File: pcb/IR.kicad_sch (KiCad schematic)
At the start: 6 parts, among them Q10 BS170, Q11 TEFT4300

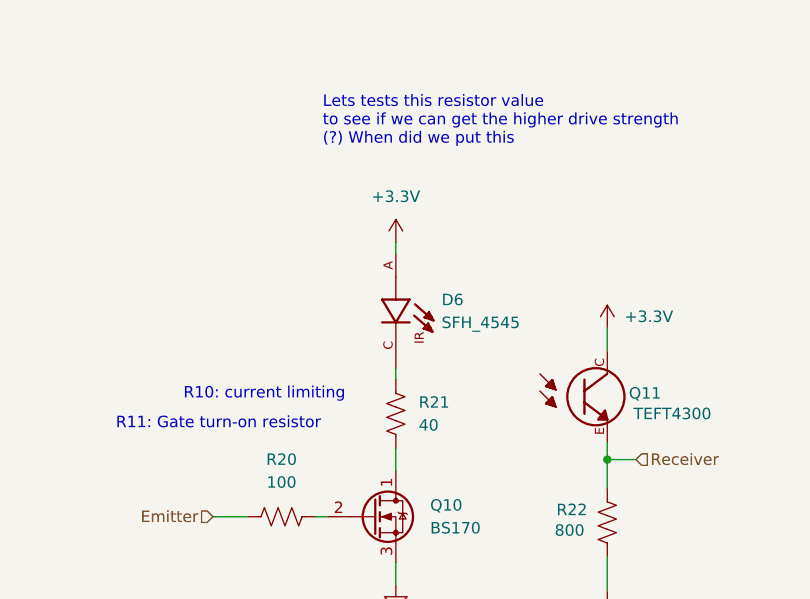
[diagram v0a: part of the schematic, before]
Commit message: changed voltage and resistor values for emitters
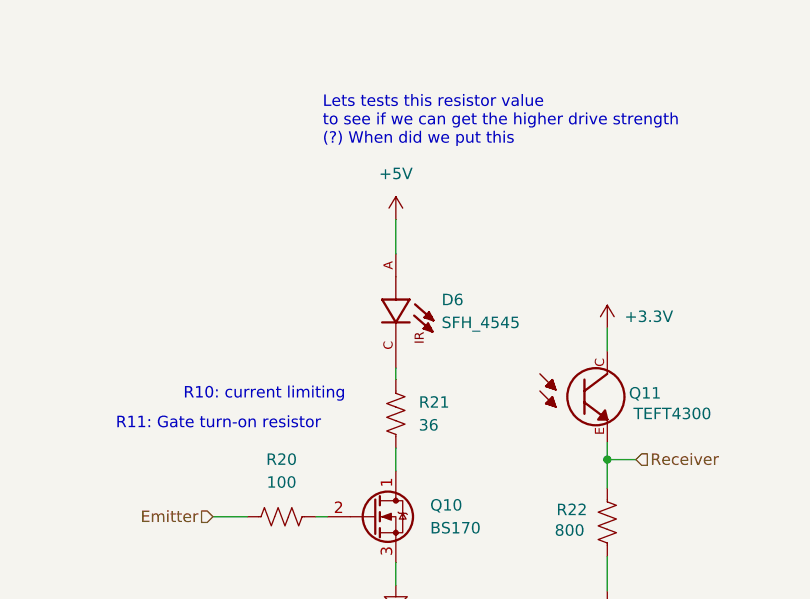
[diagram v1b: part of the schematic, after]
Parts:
- R21: value 40 -> 36
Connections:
- net +3.3V: no longer D6.A
- new net +5V: D6.A
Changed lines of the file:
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@@
 	(wire
 		(pts
-			(xy 86.36 49.53) (xy 86.36 48.26)
+			(xy 86.36 45.72) (xy 86.36 49.53)
 		)
 		(stroke
@@
 			)
 		)
-		(property "Value" "40"
+		(property "Value" "36"
 			(at 88.9 68.5799 0)
 			(show_name no)
@@
 	)
 	(symbol
-		(lib_id "power:+3.3V")
-		(at 86.36 48.26 0)
-		(unit 1)
-		(body_style 1)
-		(exclude_from_sim no)
-		(in_bom yes)
-		(on_board yes)
-		(in_pos_files yes)
-		(dnp no)
-		(fields_autoplaced yes)
-		(property "Reference" "#PWR052"
-			(at 86.36 52.07 0)
-			(hide yes)
-			(show_name no)
-			(do_not_autoplace no)
-			(effects
-				(font
-					(size 1.27 1.27)
-				)
-			)
-		)
-		(property "Value" "+3.3V"
-			(at 86.36 43.18 0)
-			(show_name no)
-			(do_not_autoplace no)
-			(effects
-				(font
-					(size 1.27 1.27)
-				)
-			)
-		)
-		(property "Footprint" ""
-			(at 86.36 48.26 0)
-			(hide yes)
-			(show_name no)
-			(do_not_autoplace no)
-			(effects
-				(font
-					(size 1.27 1.27)
-				)
-			)
-		)
-		(property "Datasheet" ""
-			(at 86.36 48.26 0)
-			(hide yes)
-			(show_name no)
-			(do_not_autoplace no)
-			(effects
-				(font
-					(size 1.27 1.27)
-				)
-			)
-		)
-		(property "Description" "Power symbol creates a global label with name \"+3.3V\""
-			(at 86.36 48.26 0)
-			(hide yes)
-			(show_name no)
-			(do_not_autoplace no)
-			(effects
-				(font
-					(size 1.27 1.27)
-				)
-			)
-		)
-		(pin "1"
-		)
-		(instances
-			(project "micromouse-pcb"
-				(path "/6bab3514-b9e6-4652-bd2e-edc57bdbde3d/1ceefd87-148b-487c-9cc8-0976f70f8c92"
-					(reference "#PWR055")
-					(unit 1)
-				)
-				(path "/6bab3514-b9e6-4652-bd2e-edc57bdbde3d/5dec74b7-7e95-4967-a373-cc0339326363"
-					(reference "#PWR063")
-					(unit 1)
-				)
-				(path "/6bab3514-b9e6-4652-bd2e-edc57bdbde3d/7f4b8bd4-4b33-4dde-a793-226b8e2de73f"
-					(reference "#PWR052")
-					(unit 1)
-				)
-				(path "/6bab3514-b9e6-4652-bd2e-edc57bdbde3d/9892aae5-d20a-4a72-957e-b0df2200cbe7"
-					(reference "#PWR059")
-					(unit 1)
-				)
-			)
-		)
-	)
-	(symbol
 		(lib_id "power:GND")
 		(at 86.36 86.36 0)
@@
 					(unit 1)
 				)
+			)
+		)
+	)
+	(symbol
+		(lib_id "power:+5V")
+		(at 86.36 45.72 0)
+		(unit 1)
+		(body_style 1)
+		(exclude_from_sim no)
+		(in_bom yes)
+		(on_board yes)
+		(in_pos_files yes)
+		(dnp no)
+		(fields_autoplaced yes)
+		(property "Reference" "#PWR02"
+			(at 86.36 49.53 0)
+			(hide yes)
+			(show_name no)
+			(do_not_autoplace no)
+			(effects
+				(font
+					(size 1.27 1.27)
+				)
+			)
+		)
+		(property "Value" "+5V"
+			(at 86.36 40.64 0)
+			(show_name no)
+			(do_not_autoplace no)
+			(effects
+				(font
+					(size 1.27 1.27)
+				)
+			)
+		)
+		(property "Footprint" ""
+			(at 86.36 45.72 0)
+			(hide yes)
+			(show_name no)
+			(do_not_autoplace no)
+			(effects
+				(font
+					(size 1.27 1.27)
+				)
+			)
+		)
+		(property "Datasheet" ""
+			(at 86.36 45.72 0)
+			(hide yes)
+			(show_name no)
+			(do_not_autoplace no)
+			(effects
+				(font
+					(size 1.27 1.27)
+				)
+			)
+		)
+		(property "Description" "Power symbol creates a global label with name \"+5V\""
+			(at 86.36 45.72 0)
+			(hide yes)
+			(show_name no)
+			(do_not_autoplace no)
+			(effects
+				(font
+					(size 1.27 1.27)
+				)
+			)
+		)
+		(pin "1"
+		)
+		(instances
+			(project "micromouse-pcb"
+				(path "/6bab3514-b9e6-4652-bd2e-edc57bdbde3d/1ceefd87-148b-487c-9cc8-0976f70f8c92"
+					(reference "#PWR06")
+					(unit 1)
+				)
+				(path "/6bab3514-b9e6-4652-bd2e-edc57bdbde3d/5dec74b7-7e95-4967-a373-cc0339326363"
+					(reference "#PWR09")
+					(unit 1)
+				)
+				(path "/6bab3514-b9e6-4652-bd2e-edc57bdbde3d/7f4b8bd4-4b33-4dde-a793-226b8e2de73f"
+					(reference "#PWR02")
+					(unit 1)
+				)
+				(path "/6bab3514-b9e6-4652-bd2e-edc57bdbde3d/9892aae5-d20a-4a72-957e-b0df2200cbe7"
+					(reference "#PWR07")
+					(unit 1)
+				)

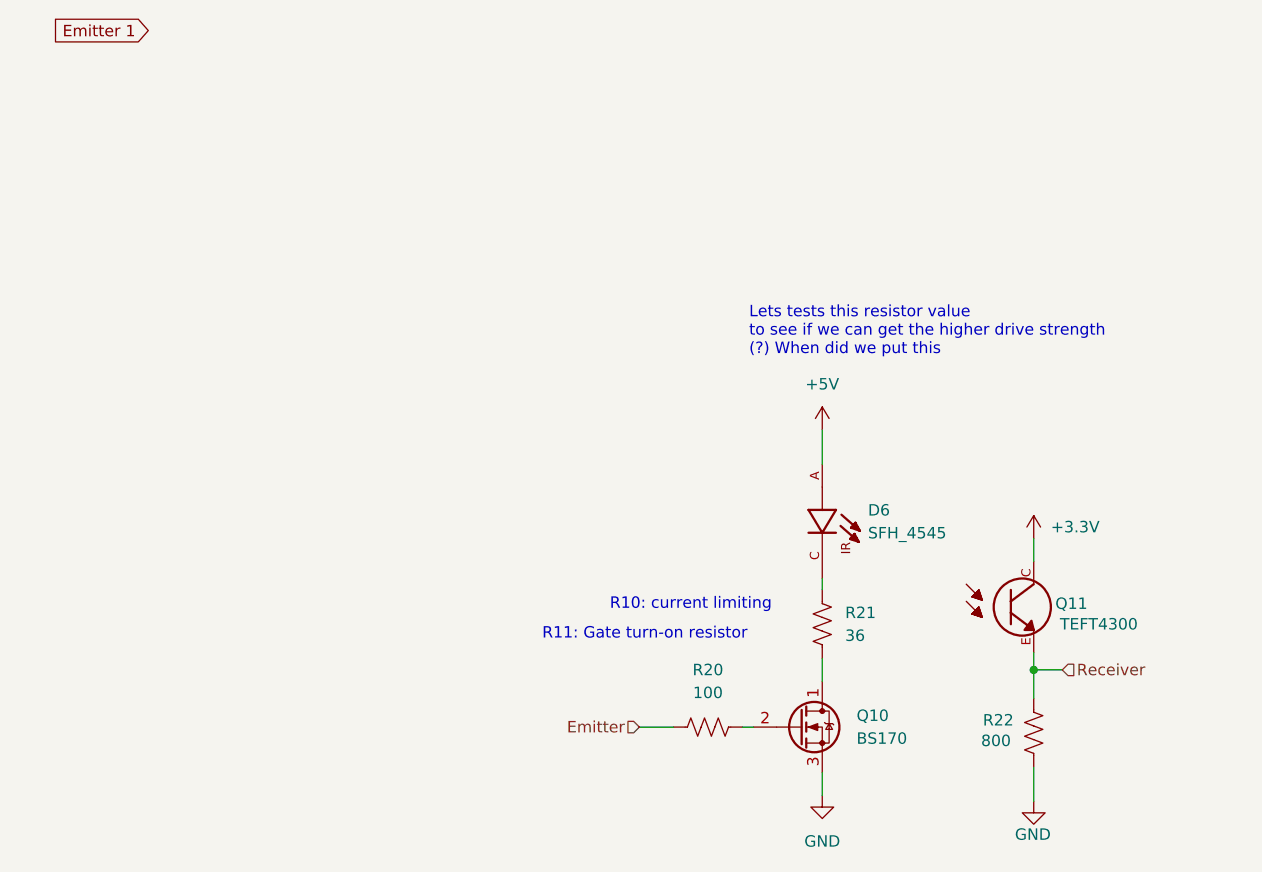
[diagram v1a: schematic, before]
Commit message: drv8833 schematic; layout component groupingi
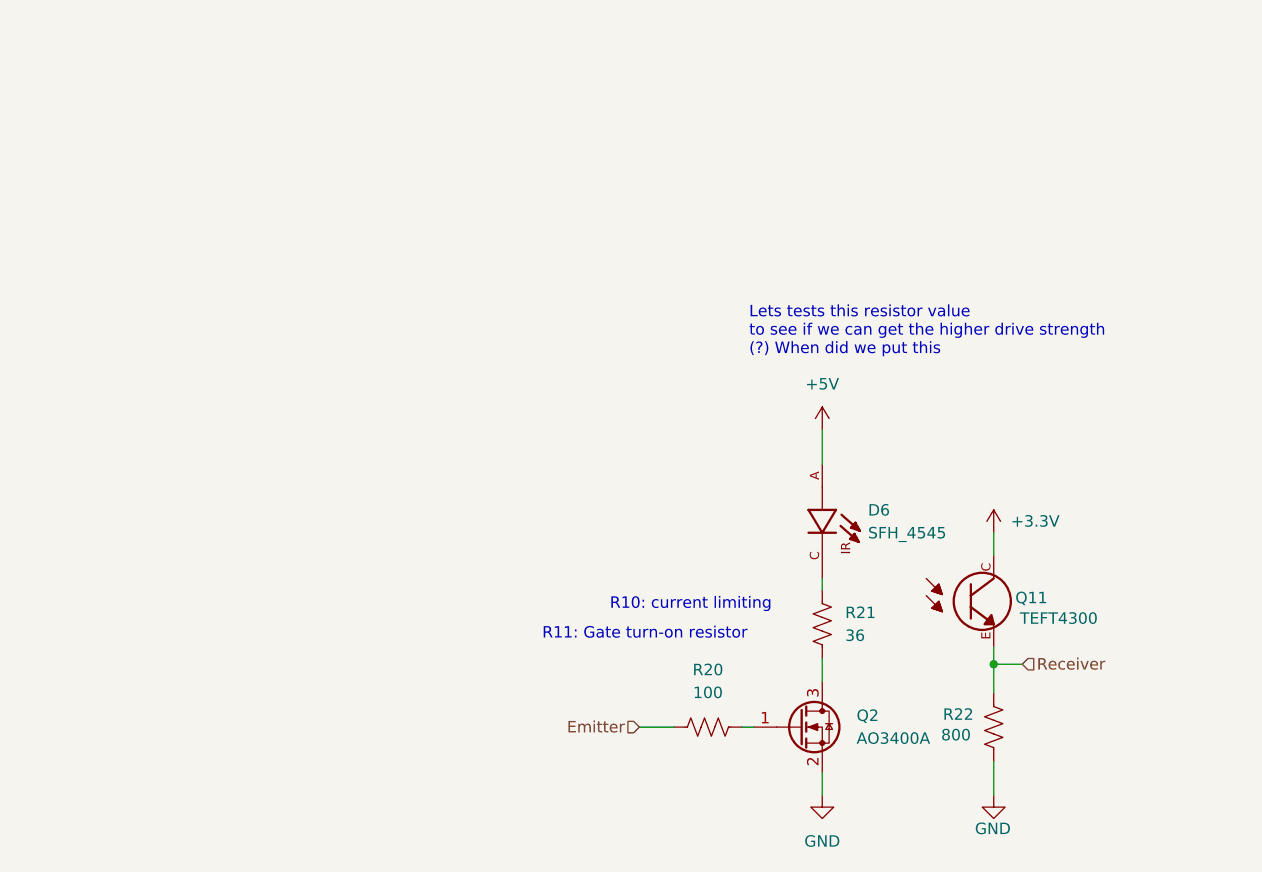
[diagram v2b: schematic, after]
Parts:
- removed Q10: BS170, Package_TO_SOT_THT:TO-92_Inline, symbol Transistor_FET:BS170
- added Q2: AO3400A, Package_TO_SOT_SMD:SOT-23_Handsoldering, symbol Transistor_FET:AO3400A
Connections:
- net GND: now also Q2.2 (S)
- net at R21.1: now also Q2.3 (D)
- net at R20.2: now also Q2.1 (G)
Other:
- moved on the sheet: Q11, R22
